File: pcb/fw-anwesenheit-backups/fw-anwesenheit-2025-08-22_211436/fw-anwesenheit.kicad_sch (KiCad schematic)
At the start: 48 parts, among them J1 Conn_01x02_Pin, J2 I2C, J3 LED, J4 MicroSD, U1 XIAO-ESP32-S3-SMD, U2 SN74AHCT1G125DBVT, U3 DS3231M

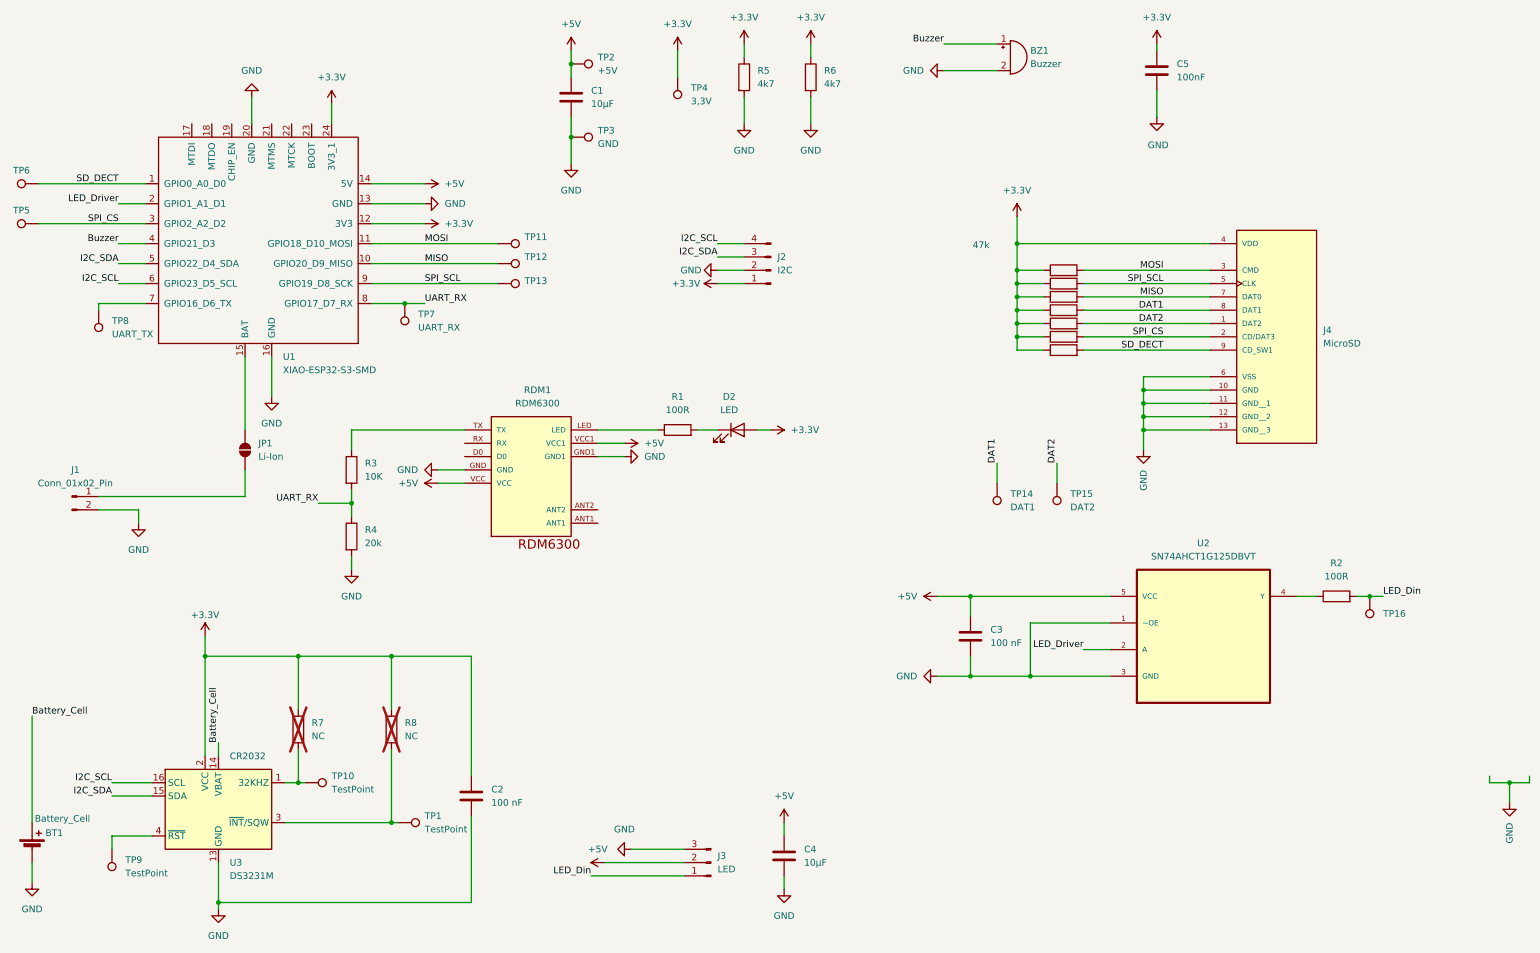
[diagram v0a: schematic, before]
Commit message: fixed RTC footprint and some labels
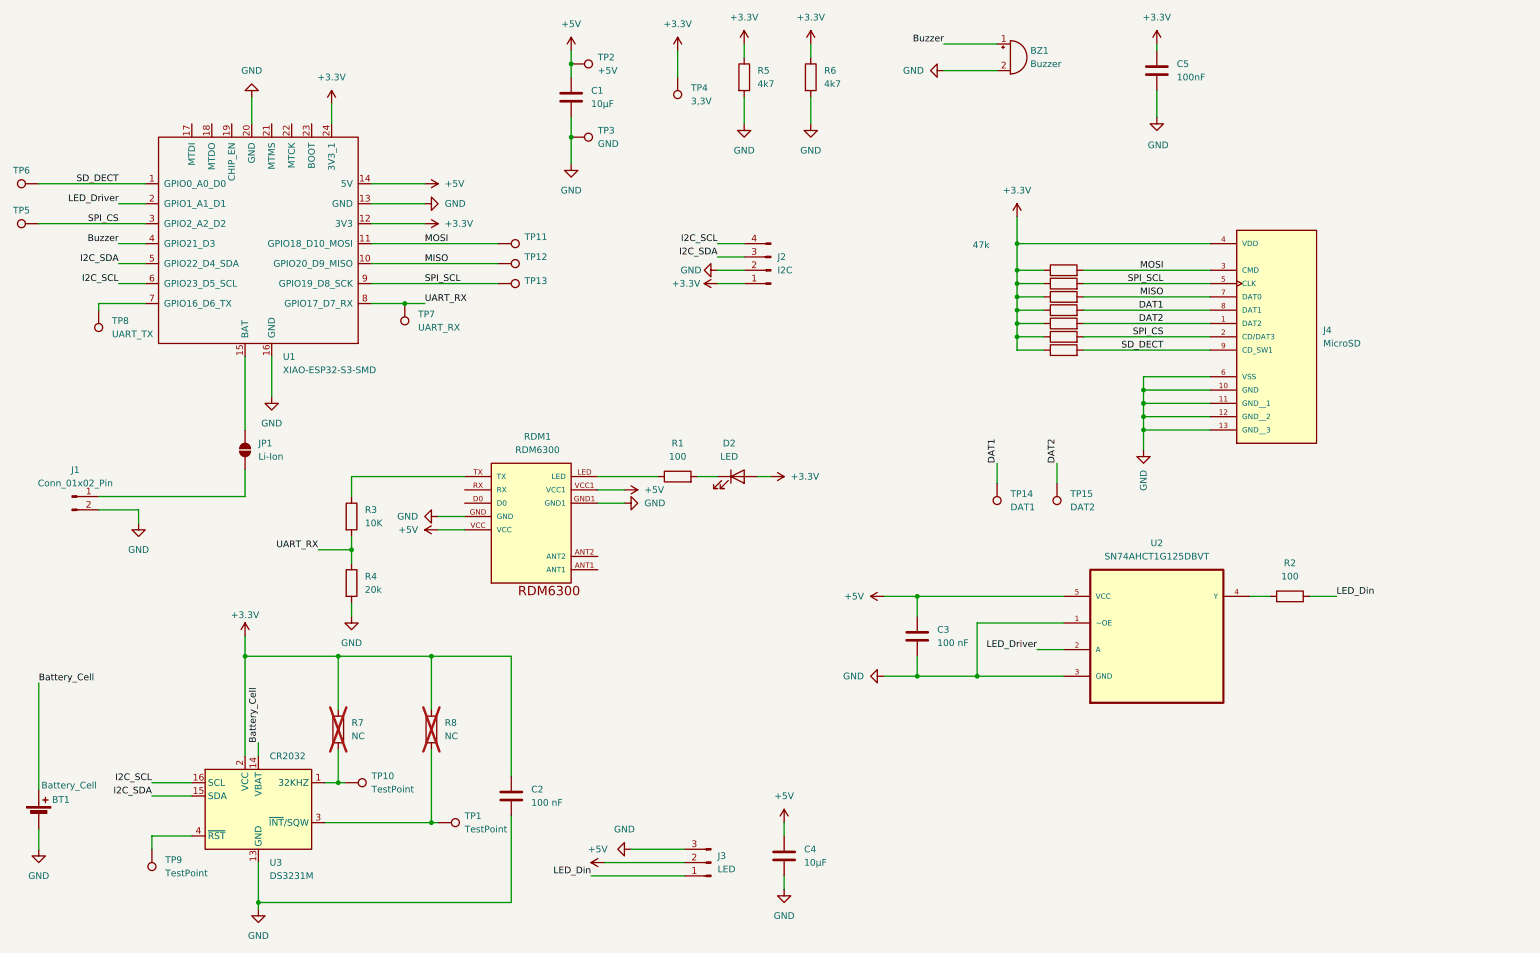
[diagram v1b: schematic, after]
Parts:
- removed TP16: LED_Din, TestPoint:TestPoint_Pad_D1.5mm, symbol Connector:TestPoint
- R1, R2: value 100R -> 100
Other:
- moved on the sheet: BT1, C2, C3, D2, R1, R2, R3, R4, R7, R8, RDM1, TP1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
